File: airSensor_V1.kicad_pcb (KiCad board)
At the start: 2 copper layers, 27 parts, among them J1 USB_C_Receptacle_USB2.0_14P, J2 Conn_01x04_Socket, SW1 SW_Push, SW2 SW_Push, SW3 SW_Push, U1 ESP32-C3-WROOM-02, U2 AP2112K-3.3, U3 SHT4x, U4 SGP40-D-R4

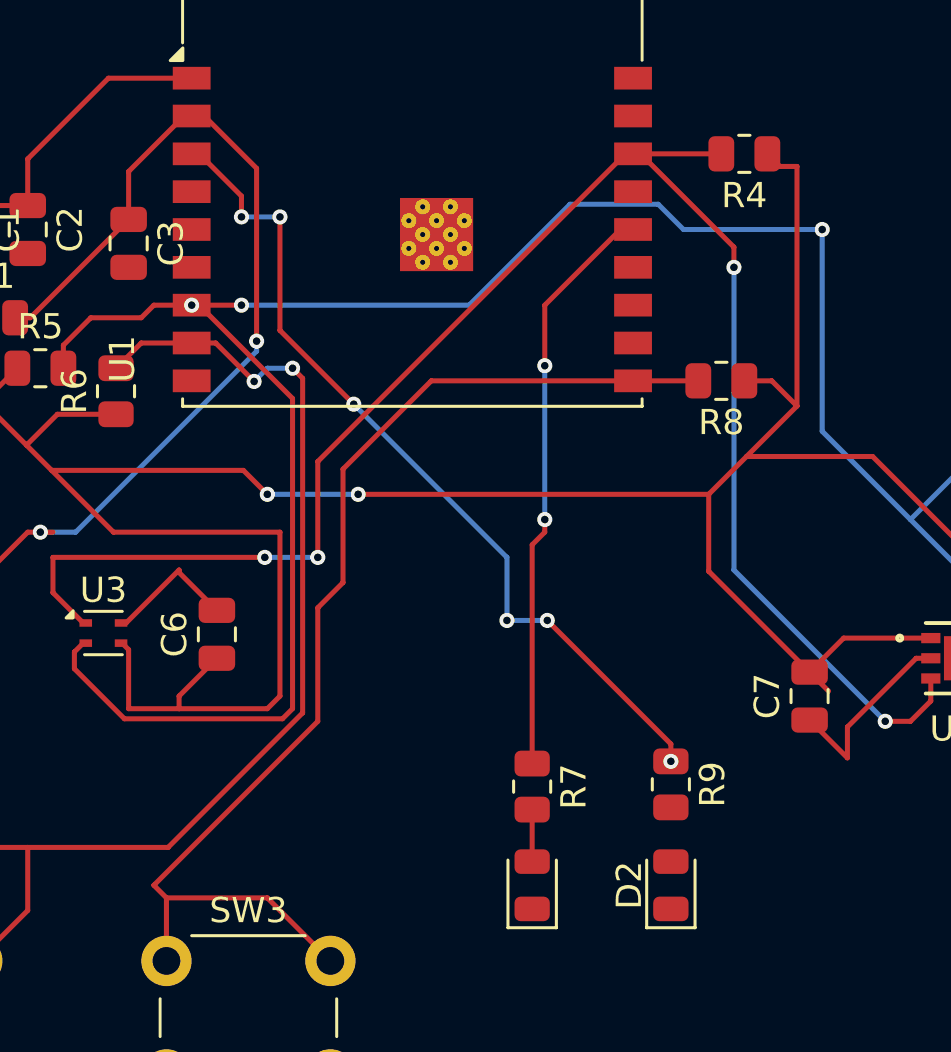
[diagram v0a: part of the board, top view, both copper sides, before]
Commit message: Updated air sensor PCB layout
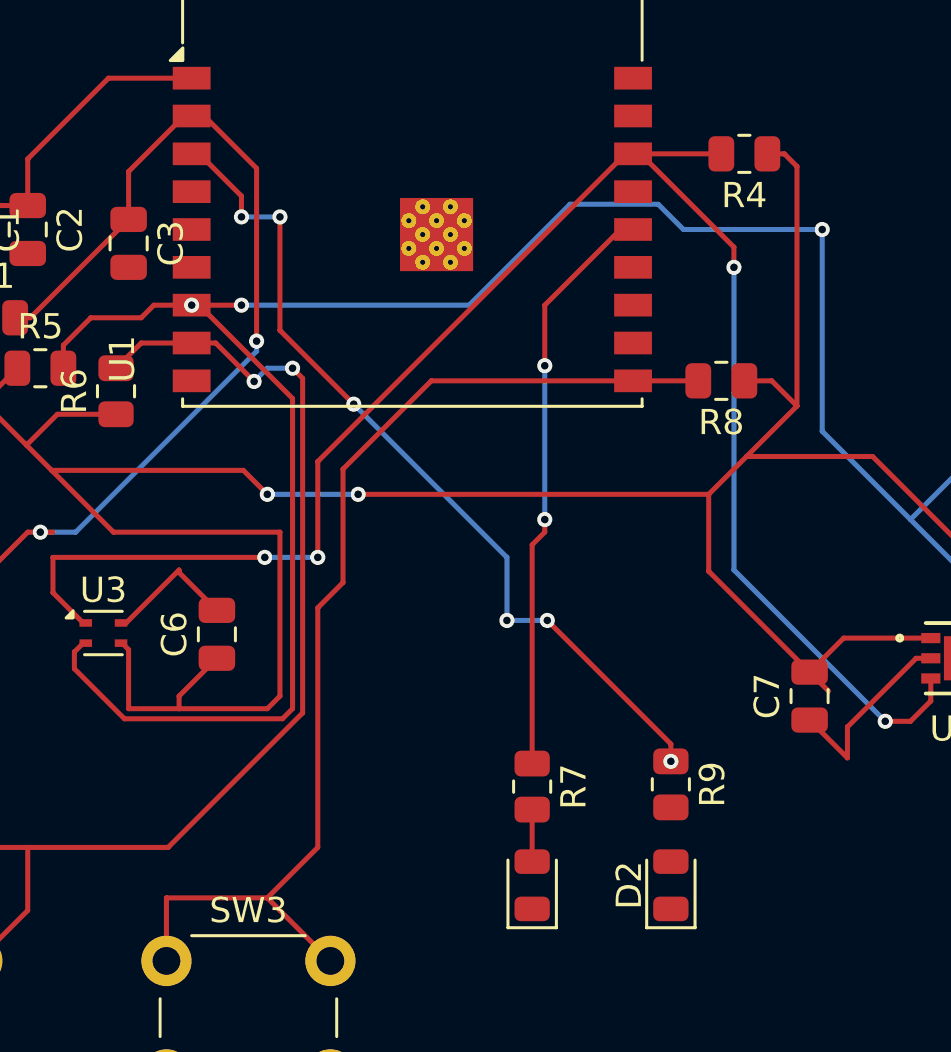
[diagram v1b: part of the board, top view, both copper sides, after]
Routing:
- net /USER_SW: track 45.9 -> 43.8 mm
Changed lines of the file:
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@@
+	)
+	(segment
+		(start 72 28)
+		(end 72.5 28.5)
+		(width 0.2)
+		(layer "F.Cu")
+		(net "+3.3V")
 	)
 	(segment
@@
 	)
 	(segment
-		(start 71.825 28.5)
-		(end 71.325 28)
-		(width 0.2)
-		(layer "F.Cu")
-		(net "+3.3V")
-	)
-	(segment
 		(start 40.2 37.8)
 		(end 39.95 37.55)
@@
 	)
 	(segment
-		(start 72.5 28.5)
-		(end 71.825 28.5)
-		(width 0.2)
-		(layer "F.Cu")
-		(net "+3.3V")
-	)
-	(segment
 		(start 70.5 40)
 		(end 72.5 38)
@@
 	)
 	(segment
+		(start 71.325 28)
+		(end 72 28)
+		(width 0.2)
+		(layer "F.Cu")
+		(net "+3.3V")
+	)
+	(segment
 		(start 42 30.05)
 		(end 42 28.2)
@@
 	)
 	(segment
+		(start 54.5 45)
+		(end 53.5 46)
+		(width 0.2)
+		(layer "F.Cu")
+		(net "/USER_SW")
+	)
+	(segment
+		(start 68.5875 37)
+		(end 66 37)
+		(width 0.2)
+		(layer "F.Cu")
+		(net "/USER_SW")
+	)
+	(segment
+		(start 58 37)
+		(end 54.5 40.5)
+		(width 0.2)
+		(layer "F.Cu")
+		(net "/USER_SW")
+	)
+	(segment
+		(start 51.5 57.5)
+		(end 54 60)
+		(width 0.2)
+		(layer "F.Cu")
+		(net "/USER_SW")
+	)
+	(segment
+		(start 47.5 57.5)
+		(end 47.5 60)
+		(width 0.2)
+		(layer "F.Cu")
+		(net "/USER_SW")
+	)
+	(segment
 		(start 54.5 40.5)
 		(end 54.5 45)
@@
 	)
 	(segment
-		(start 68.5875 37)
-		(end 66 37)
+		(start 47.5 57.5)
+		(end 51.5 57.5)
 		(width 0.2)
 		(layer "F.Cu")
@@
 	)
 	(segment
-		(start 54.5 45)
-		(end 53.5 46)
+		(start 53.5 55.5)
+		(end 51.5 57.5)
 		(width 0.2)
 		(layer "F.Cu")
@@
 	(segment
 		(start 53.5 46)
-		(end 53.5 50.5)
-		(width 0.2)
-		(layer "F.Cu")
-		(net "/USER_SW")
-	)
-	(segment
-		(start 51.5 57.5)
-		(end 54 60)
-		(width 0.2)
-		(layer "F.Cu")
-		(net "/USER_SW")
-	)
-	(segment
-		(start 47.5 57.5)
-		(end 47.5 60)
-		(width 0.2)
-		(layer "F.Cu")
-		(net "/USER_SW")
-	)
-	(segment
-		(start 53.5 50.5)
-		(end 47 57)
+		(end 53.5 55.5)
 		(width 0.2)
 		(layer "F.Cu")
@@
 		(width 0.2)
 		(layer "F.Cu")
-		(net "/USER_SW")
-	)
-	(segment
-		(start 47.5 57.5)
-		(end 51.5 57.5)
-		(width 0.2)
-		(layer "F.Cu")
-		(net "/USER_SW")
-	)
-	(segment
-		(start 47 57)
-		(end 47.5 57.5)
-		(width 0.2)
-		(layer "F.Cu")
-		(net "/USER_SW")
-	)
-	(segment
-		(start 58 37)
-		(end 54.5 40.5)
-		(width 0.2)
-		(layer "F.Cu")
